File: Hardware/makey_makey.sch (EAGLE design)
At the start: 73 parts, among them U1 ATMEGA32U4TQFP, X1 USBSMD, Y1 16MHz

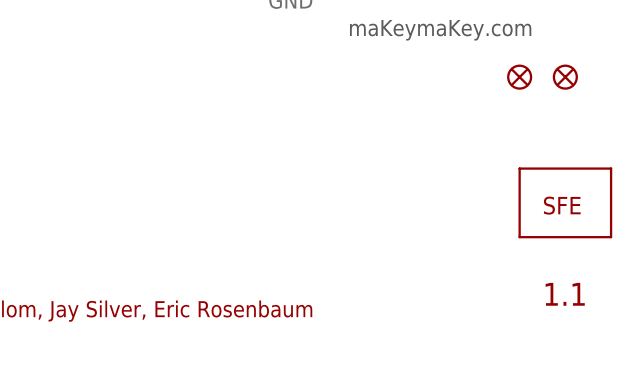
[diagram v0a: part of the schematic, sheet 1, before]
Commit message: QC Revision
1.) Switch 0402 to 0603 footprints
2.) Updated to wide PTC footprint
3.) Added more bstop over lead banks on 32u4 IC for better AOI.
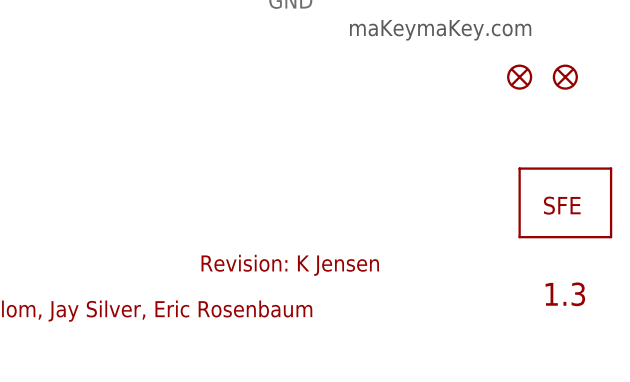
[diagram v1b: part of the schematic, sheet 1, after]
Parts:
- C1, C2, C3, C4, C5, C6, C8: device SparkFun:CAP0402-CAP -> SparkFun:CAP0603-CAP
- F1: device SparkFun-PowerIC:PTCSMD -> SparkFun-PowerIC:PTCSMD-W
- R1, R10, R11, R12, R13, R14, R15, R2, R23, R24, R25, R26, R27, R28, R29, R3, R4, R5, R6, R7, R8, R9: device SparkFun:RESISTOR0402-RES -> SparkFun:RESISTOR0603-RES
- R16, R17, R18, R19, R20, R21, R22: device SparkFun-Passives:RESISTOR0402-RES -> SparkFun-Passives:RESISTOR0603-RES
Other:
- note added: "1.3"
- note added: "Revision: K Jensen"
- note removed: "1.1"
